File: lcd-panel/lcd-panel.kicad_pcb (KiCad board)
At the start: 2 copper layers, 85 x 26 mm, 25 parts, among them J1 USB wire, J2 LCD FPC connector, J3 Fan Socket, Q1 AO3400A, U1 FT232H, U2 93LC56BT-I/OT, Y1 12.000 MHz

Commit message: Loosely throwing compononents on the PCB
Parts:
- added C12: 100nF (0.1µF), Capacitor_SMD:C_0402_1005Metric, F.Cu at (137.4, 105.8)
- added C13: 100nF (0.1µF), Capacitor_SMD:C_0402_1005Metric, F.Cu at (135.2, 107.0)
- added R6: 2.2kΩ, Resistor_SMD:R_0402_1005Metric, F.Cu at (147.1, 99.4)
- added R7: 10kΩ, Resistor_SMD:R_0402_1005Metric, F.Cu at (143.8, 101.6)
- added U3: USBLC6-2SC6, Package_TO_SOT_SMD:SOT-23-6, F.Cu at (130.7, 109.8)
- C1: value 10µF 10V -> 10 µF 10V X5R
- C2, C3: value 27pF -> 33 pF 50V C0G
- C8: value 4.7µF 10V -> 4.7 µF 16V X5R
- U1: value FT232H -> FT232HL-REEL; footprint Package_DFN_QFN:QFN-48-1EP_7x7mm_P0.5mm_EP5.15x5.15mm -> Package_QFP:LQFP-48_7x7mm_P0.5mm
- Y1: value 12.000 MHz -> 12 MHz, 20 pF load
- moved Q1 73.6 mm to (145.1, 109.7)
- moved R2 66.3 mm to (156.2, 99.7)
- moved D1 64.8 mm to (155.2, 90.0)
- moved R5 64.3 mm to (154.6, 104.5)
- moved U1 63.1 mm to (132.8, 101.0), turned to -90 degrees
- moved R3 61.2 mm to (152.7, 97.5)
- moved Y1 58.5 mm to (136.1, 90.3), turned to 180 degrees
- moved U2 57.6 mm to (143.8, 99.2), turned to 180 degrees
- moved C11 57.1 mm to (139.1, 105.5), turned to 90 degrees
- moved C6 56.0 mm to (138.8, 98.7), turned to 90 degrees
- moved C1 54.6 mm to (140.8, 103.1), turned to -90 degrees
- moved C3 54.3 mm to (139.2, 90.0), turned to -90 degrees
- moved C5 53.6 mm to (127.8, 104.8), turned to 180 degrees
- moved R4 52.7 mm to (135.2, 108.2)
- moved C8 51.1 mm to (139.1, 102.3), turned to 90 degrees
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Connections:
- C1 pad 1: unconnected-(C1-Pad1) -> +5V
- C1 pad 2: unconnected-(C1-Pad2) -> GND
- C10 pad 1: unconnected-(C10-Pad1) -> GND
- C10 pad 2: unconnected-(C10-Pad2) -> +3V3
- C11 pad 1: unconnected-(C11-Pad1) -> GND
- C11 pad 2: unconnected-(C11-Pad2) -> Net-(U1-VCCCORE)
- C2 pad 1: unconnected-(C2-Pad1) -> Net-(U1-XCSO)
- C2 pad 2: unconnected-(C2-Pad2) -> GND
- C3 pad 1: unconnected-(C3-Pad1) -> Net-(U1-XCSI)
- C3 pad 2: unconnected-(C3-Pad2) -> GND
- C4 pad 1: unconnected-(C4-Pad1) -> +3V3
- C4 pad 2: unconnected-(C4-Pad2) -> GND
- C5 pad 1: unconnected-(C5-Pad1) -> +3V3
- C5 pad 2: unconnected-(C5-Pad2) -> GND
- C6 pad 1: unconnected-(C6-Pad1) -> +3V3
- C6 pad 2: unconnected-(C6-Pad2) -> GND
- C7 pad 1: unconnected-(C7-Pad1) -> GND
- C7 pad 2: unconnected-(C7-Pad2) -> +3V3
- C8 pad 1: unconnected-(C8-Pad1) -> +3V3
- C8 pad 2: unconnected-(C8-Pad2) -> GND
- C9 pad 1: unconnected-(C9-Pad1) -> +5V
- C9 pad 2: unconnected-(C9-Pad2) -> GND
- D1 pad 1: unconnected-(D1-K-Pad1) -> +5V
- D1 pad 2: unconnected-(D1-A-Pad2) -> Net-(D1-A)
- FB1 pad 1: unconnected-(FB1-Pad1) -> VBUS
- FB1 pad 2: unconnected-(FB1-Pad2) -> +5V
- J1 pad 1: unconnected-(J1-Pin_1-Pad1) -> VBUS
- J1 pad 2: unconnected-(J1-Pin_2-Pad2) -> USB_D-
- J1 pad 3: unconnected-(J1-Pin_3-Pad3) -> USB_D+
- J1 pad 4: unconnected-(J1-Pin_4-Pad4) -> GND
- J1 pad MP: unconnected-(J1-MountPin-PadMP) -> GND
- J2 pad 1: unconnected-(J2-Pin_1-Pad1) -> LCD_MOSI
- J2 pad 10: (no net) -> GND
- J2 pad 2: unconnected-(J2-Pin_2-Pad2) -> LCD_SCK
- J2 pad 3: unconnected-(J2-Pin_3-Pad3) -> LCD_DC
- J2 pad 4: unconnected-(J2-Pin_4-Pad4) -> LCD_RST
- J2 pad 5: unconnected-(J2-Pin_5-Pad5) -> LCD_CS
- J2 pad 7: unconnected-(J2-Pin_7-Pad7) -> +3V3
- J2 pad 8: (no net) -> GND
- J2 pad 9: (no net) -> LCD_BL
- J2 pad MP: unconnected-(J2-MountPin-PadMP) -> GND
- J3 pad 1: unconnected-(J3-Pin_1-Pad1) -> Net-(D1-A)
- J3 pad 2: unconnected-(J3-Pin_2-Pad2) -> +5V
- J3 pad 3: unconnected-(J3-Pin_3-Pad3) -> FAN TACH
- Q1 pad 1: unconnected-(Q1-G-Pad1) -> Net-(Q1-G)
- Q1 pad 2: unconnected-(Q1-S-Pad2) -> GND
- Q1 pad 3: unconnected-(Q1-D-Pad3) -> Net-(D1-A)
- R1 pad 1: unconnected-(R1-Pad1) -> GND
- R1 pad 2: unconnected-(R1-Pad2) -> Net-(U1-REF)
- R2 pad 1: unconnected-(R2-Pad1) -> FAN GATE
- R2 pad 2: unconnected-(R2-Pad2) -> Net-(Q1-G)
- R3 pad 1: unconnected-(R3-Pad1) -> Net-(Q1-G)
- R3 pad 2: unconnected-(R3-Pad2) -> GND
- R4 pad 1: unconnected-(R4-Pad1) -> RESET
- R4 pad 2: unconnected-(R4-Pad2) -> +3V3
- R5 pad 1: unconnected-(R5-Pad1) -> FAN TACH
- R5 pad 2: unconnected-(R5-Pad2) -> +3V3
- U1 pad 1: unconnected-(U1-XCSI-Pad1) -> Net-(U1-XCSI)
- U1 pad 10: unconnected-(U1-GND-Pad10) -> GND
- U1 pad 11: unconnected-(U1-GND-Pad11) -> GND
- U1 pad 12: unconnected-(U1-VCCIO-Pad12) -> +3V3
- U1 pad 13: unconnected-(U1-ADBUS0-Pad13) -> LCD_SCK
- U1 pad 14: unconnected-(U1-ADBUS1-Pad14) -> LCD_MOSI
- U1 pad 16: unconnected-(U1-ADBUS3-Pad16) -> LCD_CS
- U1 pad 17: unconnected-(U1-ADBUS4-Pad17) -> LCD_DC
- U1 pad 18: unconnected-(U1-ADBUS5-Pad18) -> LCD_RST
- U1 pad 19: unconnected-(U1-ADBUS6-Pad19) -> LCD_BL
- U1 pad 2: unconnected-(U1-XCSO-Pad2) -> Net-(U1-XCSO)
- U1 pad 20: unconnected-(U1-ADBUS7-Pad20) -> FAN GATE
- U1 pad 21: unconnected-(U1-ACBUS0-Pad21) -> FAN TACH
- U1 pad 22: unconnected-(U1-GND-Pad22) -> GND
- U1 pad 23: unconnected-(U1-GND-Pad23) -> GND
- U1 pad 24: unconnected-(U1-VCCIO-Pad24) -> +3V3
- U1 pad 3: unconnected-(U1-VPHY-Pad3) -> +3V3
- U1 pad 34: unconnected-(U1-~{RESET}-Pad34) -> RESET
- U1 pad 35: unconnected-(U1-GND-Pad35) -> GND
- U1 pad 36: unconnected-(U1-GND-Pad36) -> GND
- U1 pad 37: unconnected-(U1-VCCA-Pad37) -> Net-(U1-VCCA)
- U1 pad 38: unconnected-(U1-VCCCORE-Pad38) -> Net-(U1-VCCCORE)
- U1 pad 39: unconnected-(U1-VCCD-Pad39) -> +3V3
- U1 pad 4: unconnected-(U1-AGND-Pad4) -> GND
- U1 pad 40: unconnected-(U1-VREGIN-Pad40) -> +5V
- U1 pad 41: unconnected-(U1-AGND-Pad41) -> GND
- U1 pad 42: unconnected-(U1-TEST-Pad42) -> GND
- U1 pad 43: unconnected-(U1-EEDATA-Pad43) -> EEDATA
- U1 pad 44: unconnected-(U1-EECLK-Pad44) -> EECLK
- U1 pad 45: unconnected-(U1-EECS-Pad45) -> EECS
- U1 pad 46: unconnected-(U1-VCCIO-Pad46) -> +3V3
- U1 pad 47: unconnected-(U1-GND-Pad47) -> GND
- U1 pad 48: unconnected-(U1-GND-Pad48) -> GND
- U1 pad 5: unconnected-(U1-REF-Pad5) -> Net-(U1-REF)
- U1 pad 6: unconnected-(U1-DM-Pad6) -> D-
- U1 pad 7: unconnected-(U1-DP-Pad7) -> D+
- U1 pad 8: unconnected-(U1-VPLL-Pad8) -> +3V3
- U1 pad 9: unconnected-(U1-AGND-Pad9) -> GND
- U2 pad 1: unconnected-(U2-DO-Pad1) -> Net-(U2-DO)
- U2 pad 2: unconnected-(U2-GND-Pad2) -> GND
- U2 pad 3: unconnected-(U2-DI-Pad3) -> EEDATA
- U2 pad 4: unconnected-(U2-CLK-Pad4) -> EECLK
- U2 pad 5: unconnected-(U2-CS-Pad5) -> EECS
- U2 pad 6: unconnected-(U2-VCC-Pad6) -> +3V3
- Y1 pad 1: unconnected-(Y1-Pad1) -> Net-(U1-XCSI)
- Y1 pad 2: unconnected-(Y1-Pad2) -> GND
- Y1 pad 3: unconnected-(Y1-Pad3) -> Net-(U1-XCSO)
- Y1 pad 4: unconnected-(Y1-Pad4) -> GND
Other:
- outline, holes or cut-outs redrawn

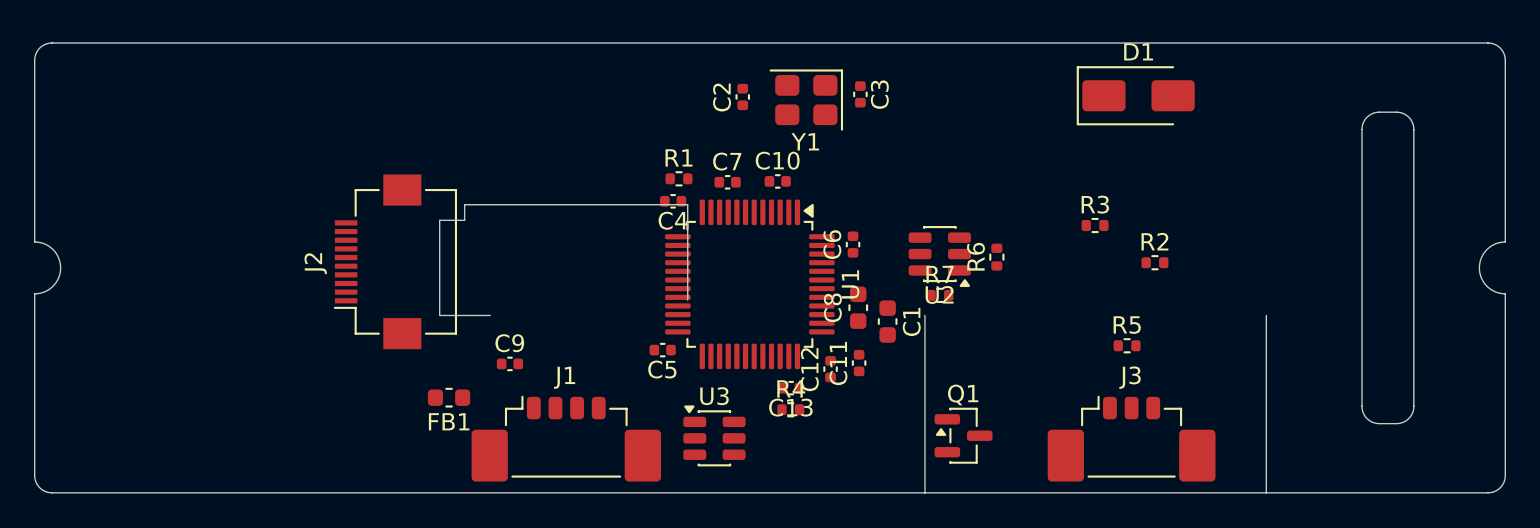
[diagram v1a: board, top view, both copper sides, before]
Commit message: Moving components to their proper positions
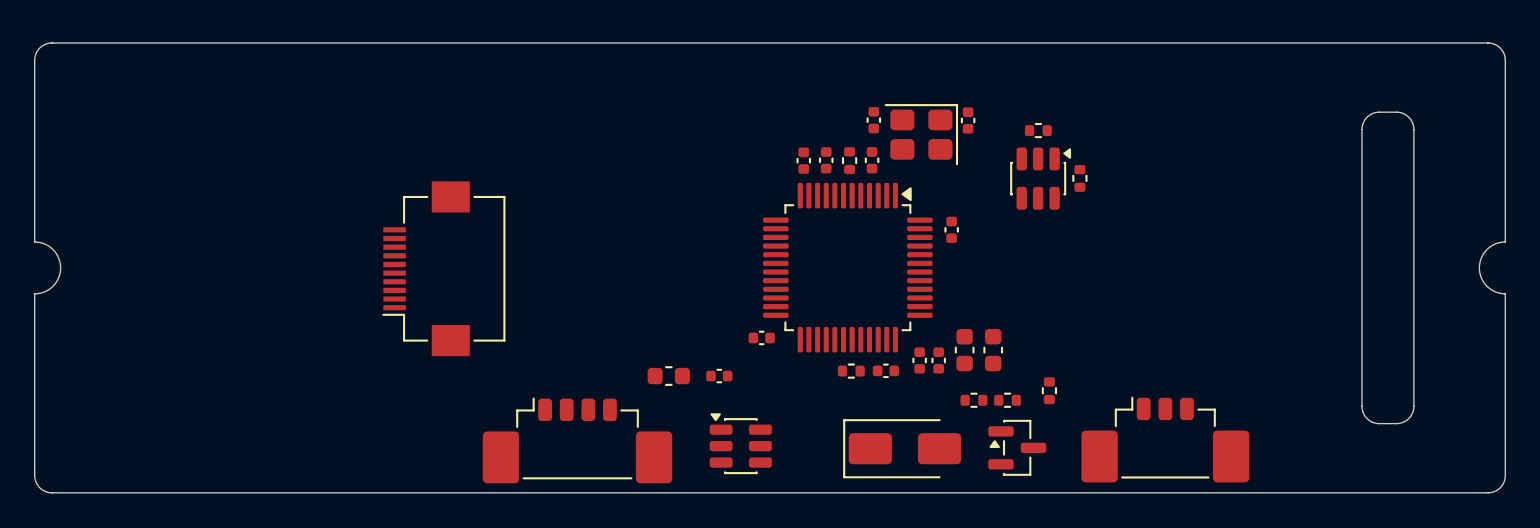
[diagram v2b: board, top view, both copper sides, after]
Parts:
- moved D1 24.5 mm to (141.8, 110.5)
- moved R2 13.1 mm to (145.7, 107.7)
- moved FB1 12.8 mm to (128.1, 106.2), turned to 0 degrees
- moved C9 12.1 mm to (131.0, 106.2)
- moved R3 11.3 mm to (147.7, 107.7)
- moved R7 10.5 mm to (151.9, 94.8), turned to 90 degrees
- moved R1 9.92 mm to (138.6, 93.8), turned to -90 degrees
- moved C4 7.91 mm to (135.9, 93.8), turned to 90 degrees
- moved R6 7.70 mm to (149.5, 92.1), turned to 180 degrees
- moved C2 7.69 mm to (139.9, 91.5)
- moved U2 7.17 mm to (149.4, 94.8), turned to -90 degrees
- moved Y1 6.94 mm to (142.7, 92.3)
- moved C8 6.62 mm to (145.2, 104.8), turned to -90 degrees
- moved C3 6.41 mm to (145.4, 91.5)
- moved C1 6.32 mm to (146.8, 104.8)
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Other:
- outline, holes or cut-outs redrawn

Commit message: Hooking up most of the wiring
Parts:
- moved C6 1.70 mm to (144.4, 96.1)
- moved U2 1.08 mm to (149.7, 93.8)
- moved R6 1.08 mm to (149.7, 91.0)
- moved R7 1.08 mm to (152.1, 93.8)
- moved C5 0.59 mm to (133.9, 104.5), turned to -90 degrees
- moved R2 0.25 mm to (145.7, 107.9)
- moved R3 0.25 mm to (147.7, 107.9)
- moved C1 0.15 mm to (147.0, 104.8)
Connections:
- J3 pad MP: unconnected-(J3-MountPin-PadMP) -> GND
- U1 pad 17: LCD_DC -> LCD_BL
- U1 pad 19: LCD_BL -> LCD_DC
- U1 pad 21: FAN TACH -> unconnected-(U1-ACBUS0-Pad21)
- U1 pad 25: unconnected-(U1-ACBUS1-Pad25) -> FAN TACH
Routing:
- net +3V3: track 0.00 -> 94.2 mm, vias 0 -> 2
- net +5V: track 0.00 -> 56.8 mm, vias 0 -> 2
- net FAN TACH: track 0.00 -> 25.2 mm
- net LCD_MOSI: track 0.00 -> 24.2 mm, vias 0 -> 2
- net LCD_SCK: track 0.00 -> 24.0 mm, vias 0 -> 2
- net LCD_CS: track 0.00 -> 22.7 mm
- net LCD_BL: track 0.00 -> 22.5 mm, vias 0 -> 2
- net LCD_RST: track 0.00 -> 22.5 mm
- net LCD_DC: track 0.00 -> 22.5 mm
- net FAN GATE: track 0.00 -> 20.0 mm
- net D+: track 0.00 -> 19.3 mm, vias 0 -> 2
- net D-: track 0.00 -> 18.3 mm, vias 0 -> 2
- net GND: track 0.00 -> 17.4 mm, vias 0 -> 22
- net EEDATA: track 0.00 -> 13.5 mm, vias 0 -> 2
- net Net-(D1-A): track 0.00 -> 12.8 mm
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- added copper zone on B.Cu, net GND
- added copper zone on F.Cu, net GND

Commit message: Mostly spit an polish
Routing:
- net GND: track 17.4 -> 41.6 mm, vias 22 -> 23
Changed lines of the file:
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@@
+	)
+	(segment
+		(start 147.15 111.2)
+		(end 147.3 111.35)
+		(width 0.2)
+		(layer "F.Cu")
+		(net 11)
+	)
+	(segment
+		(start 141.6 91.45)
+		(end 141.6 89.7)
+		(width 0.2)
+		(layer "F.Cu")
+		(net 11)
+	)
+	(segment
+		(start 145.85 111.2)
+		(end 147.15 111.2)
+		(width 0.2)
+		(layer "F.Cu")
+		(net 11)
+	)
+	(segment
+		(start 147 105.525)
+		(end 148.475 105.525)
+		(width 0.2)
+		(layer "F.Cu")
+		(net 11)
+	)
+	(segment
+		(start 128.25 103.55)
+		(end 129.45 103.55)
+		(width 0.2)
+		(layer "F.Cu")
+		(net 11)
+	)
+	(segment
+		(start 142.6125 97.2375)
+		(end 142.6125 96.0375)
+		(width 0.2)
+		(layer "F.Cu")
+		(net 11)
 	)
 	(segment
@@
 	)
 	(segment
+		(start 140.1 97.499265)
+		(end 140.099265 97.499265)
+		(width 0.2)
+		(layer "F.Cu")
+		(net 11)
+	)
+	(segment
 		(start 141.13 105.95)
 		(end 141.75 105.95)
@@
 	)
 	(segment
+		(start 138.52 93.32)
+		(end 138.55 93.29)
+		(width 0.2)
+		(layer "F.Cu")
+		(net 11)
+	)
+	(segment
 		(start 142.58 105.85)
 		(end 142.6 105.83)
@@
 	)
 	(segment
+		(start 124.7 108.2)
+		(end 127.95 108.2)
+		(width 0.2)
+		(layer "F.Cu")
+		(net 11)
+	)
+	(segment
 		(start 142.6125 100.7375)
 		(end 144.1625 100.7375)
@@
 	)
 	(segment
+		(start 148.19 107.9)
+		(end 148.6 107.9)
+		(width 0.2)
+		(layer "F.Cu")
+		(net 11)
+	)
+	(segment
 		(start 132.9 102.35)
 		(end 133.0125 102.2375)
@@
 	)
 	(segment
+		(start 112.25 97.8)
+		(end 112.25 96.7)
+		(width 0.2)
+		(layer "F.Cu")
+		(net 11)
+	)
+	(segment
+		(start 136.2 95.825)
+		(end 137.2 95.825)
+		(width 0.2)
+		(layer "F.Cu")
+		(net 11)
+	)
+	(segment
 		(start 130.5 110.3)
 		(end 129.5 109.3)
@@
 	)
 	(segment
+		(start 142.6125 96.0375)
+		(end 142.85 95.8)
+		(width 0.2)
+		(layer "F.Cu")
+		(net 11)
+	)
+	(segment
+		(start 129.45 103.55)
+		(end 131.5 105.6)
+		(width 0.2)
+		(layer "F.Cu")
+		(net 11)
+	)
+	(segment
+		(start 139.7 97.1)
+		(end 139.7 95.825)
+		(width 0.2)
+		(layer "F.Cu")
+		(net 11)
+	)
+	(segment
 		(start 141.2 104.15)
 		(end 141.2 105.88)
@@
 	)
 	(segment
+		(start 131.5 105.6)
+		(end 131.5 106.25)
+		(width 0.2)
+		(layer "F.Cu")
+		(net 11)
+	)
+	(segment
 		(start 141.2 105.88)
 		(end 141.13 105.95)
@@
 	)
 	(segment
+		(start 139.84 93.29)
+		(end 139.85 93.3)
+		(width 0.2)
+		(layer "F.Cu")
+		(net 11)
+	)
+	(segment
 		(start 134.2875 101.7375)
 		(end 134.2875 102.2375)
@@
 	)
 	(segment
+		(start 138.55 93.29)
+		(end 139.84 93.29)
+		(width 0.2)
+		(layer "F.Cu")
+		(net 11)
+	)
+	(segment
 		(start 141.85 105.85)
 		(end 142.58 105.85)
@@
 	)
 	(segment
-		(start 139.7 95.825)
-		(end 139.7 97.25)
+		(start 148.475 105.525)
+		(end 148.5 105.5)
 		(width 0.2)
 		(layer "F.Cu")
@@
 	)
 	(segment
-		(start 136.2 95.825)
-		(end 137.2 95.825)
+		(start 112.25 98.8)
+		(end 110.75 98.8)
+		(width 0.2)
+		(layer "F.Cu")
+		(net 11)
+	)
+	(segment
+		(start 135.9 93.32)
+		(end 138.52 93.32)
 		(width 0.2)
 		(layer "F.Cu")
@@
 	)
 	(segment
+		(start 112.25 97.8)
+		(end 110.75 97.8)
+		(width 0.2)
+		(layer "F.Cu")
+		(net 11)
+	)
+	(segment
 		(start 133.0125 102.2375)
 		(end 134.2875 102.2375)
@@
 	)
 	(segment
+		(start 127.95 108.2)
+		(end 128 108.15)
+		(width 0.2)
+		(layer "F.Cu")
+		(net 11)
+	)
+	(segment
 		(start 141.75 105.95)
 		(end 141.85 105.85)
@@
 	)
 	(segment
+		(start 140.099265 97.499265)
+		(end 139.7 97.1)
+		(width 0.2)
+		(layer "F.Cu")
+		(net 11)
+	)
+	(segment
 		(start 131.125 110.3)
 		(end 130.5 110.3)
@@
 	)
 	(segment
+		(start 148.6 107.9)
+		(end 149.45 108.75)
+		(width 0.2)
+		(layer "F.Cu")
+		(net 11)
+	)
+	(segment
 		(start 142.6125 97.7375)
 		(end 142.6125 97.2375)
@@
 		(net 11)
 	)
-	(segment
-		(start 139.7 97.25)
-		(end 139.95 97.5)
-		(width 0.2)
-		(layer "F.Cu")
-		(net 11)
-	)
 	(via
 		(at 122.7 97.8)
@@
 	)
 	(via
+		(at 141.6 89.7)
+		(size 0.6)
+		(drill 0.3)
+		(layers "F.Cu" "B.Cu")
+		(free yes)
+		(net 11)
+	)
+	(via
 		(at 142.85 95.8)
 		(size 0.6)
@@
 	)
 	(via
-		(at 139.95 97.5)
+		(at 140.1 97.499265)
 		(size 0.6)
 		(drill 0.3)
@@
 	)
 	(via
-		(at 138.3 97.5)
+		(at 138.3 97.499633)
 		(size 0.6)
 		(drill 0.3)
@@
 	)
 	(segment
+		(start 139.25 97.4)
+		(end 138.7 96.85)
+		(width 0.2)
+		(layer "F.Cu")
+		(net 37)
+	)
+	(segment
+		(start 139.25 97.498438)
+		(end 139.25 97.4)
+		(width 0.2)
+		(layer "F.Cu")
+		(net 37)
+	)
+	(segment
+		(start 139.098438 97.65)
+		(end 139.25 97.498438)
+		(width 0.2)
+		(layer "F.Cu")
+		(net 37)
+	)
+	(segment
 		(start 137.2 109.35)
 		(end 137.25 109.3)
@@
 	)
 	(segment
-		(start 138.7 96.596324)
+		(start 138.7 96.85)
 		(end 138.7 95.825)
 		(width 0.2)
@@
 		(net 37)
 	)
-	(segment
-		(start 139.098438 96.994762)
-		(end 138.7 96.596324)
-		(width 0.2)
-		(layer "F.Cu")
-		(net 37)
-	)
-	(segment
-		(start 139.098438 97.65)
-		(end 139.098438 96.994762)
-		(width 0.2)
-		(layer "F.Cu")
-		(net 37)
-	)
-	(via
-		(at 139.098438 97.5)
-		(size 0.6)
-		(drill 0.3)
+	(via
+		(at 139.25 97.5)
+		(size 0.6)
+		(drill 0.3)
